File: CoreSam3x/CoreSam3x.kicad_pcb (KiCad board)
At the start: 2 copper layers, 50.8 x 50.8 mm, 65 parts, among them M1 PCB_GREEN_RMC, P1 HDR, P2 HDR, P3 HDR, P4 HDR, P5 HDR, P6 HDR, P8 HDR, Q1 BSS123, U1 ATSAM3X8E, U2 LM1117MP-3.3, U3 USBCONN-HOSTCAPABLE, U4 SP2525A, X1 CRYSTAL_4PIN, X2 32kHz

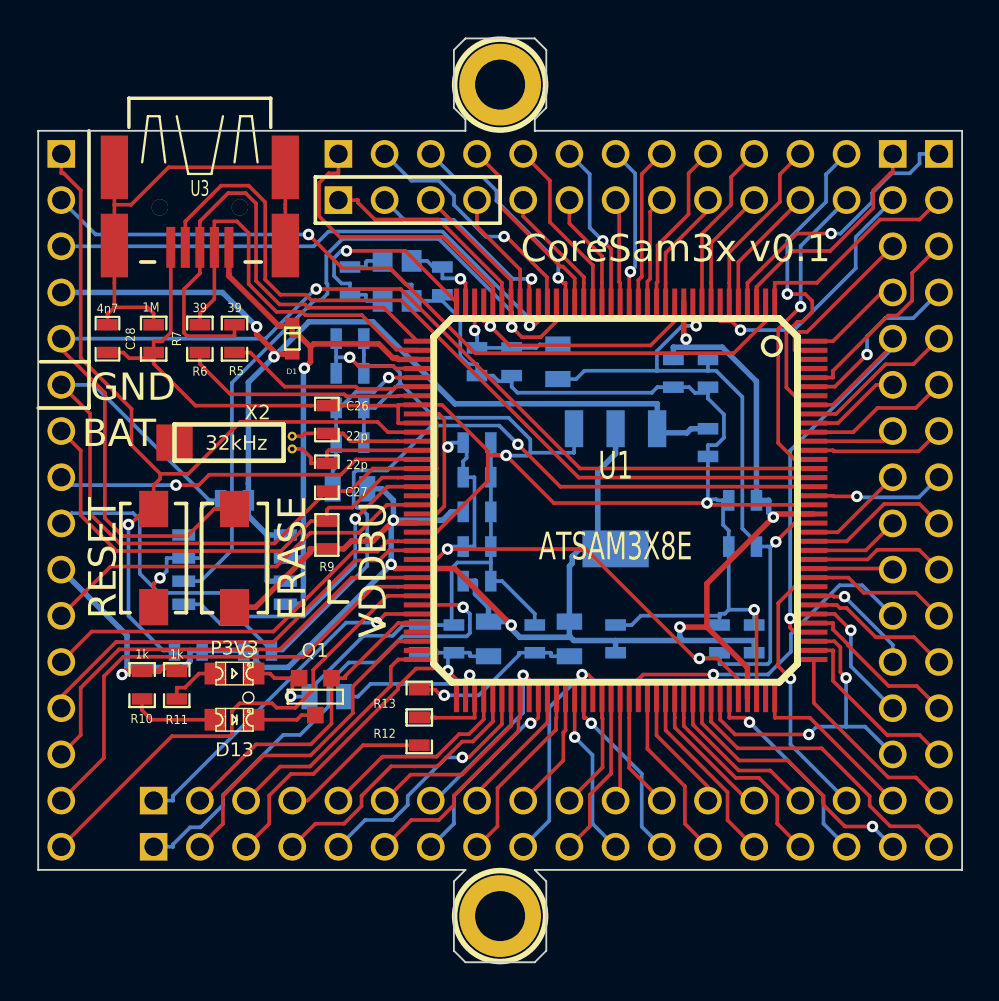
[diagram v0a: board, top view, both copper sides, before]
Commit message: CoreSam3x: improvements to layout, component selection
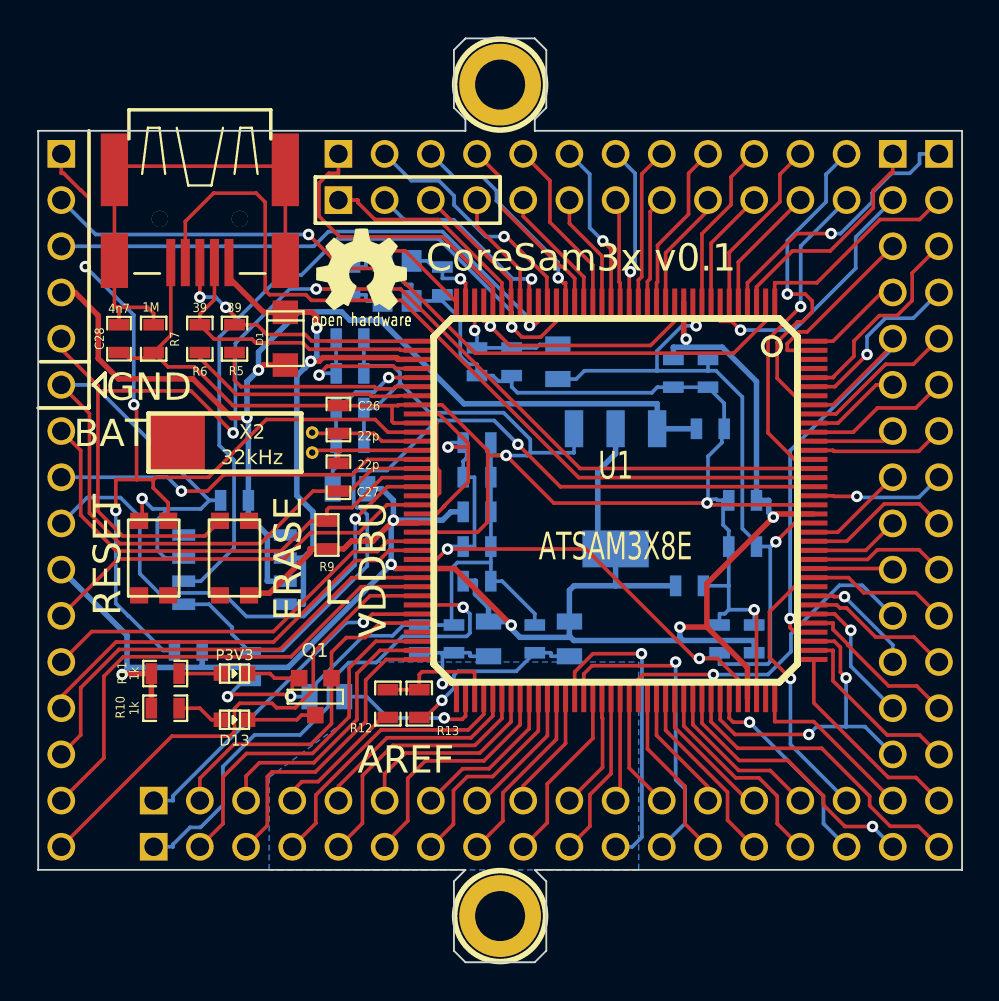
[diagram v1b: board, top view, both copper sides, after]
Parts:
- added M2: LOGO_OSHW, Logo_silk_OSHW_6x6mm, F.Cu at (58.4, 96.5)
- D1: footprint sod523 -> do219ab
- D2: footprint LED-0805_BLUE -> Led_0603
- D3: footprint LED-0805_GREEN -> Led_0603
- R8: value 100k -> 10k
- S1, S2: footprint SW_APEM_ADTSM3 -> SW_C&K_KMR4
- U4: value SP2525A -> SP2525A-1EN
- X2: footprint crystal_tc-26_horiz -> crystal_tc-38_horiz_RMC
- moved C25 5.00 mm to (76.5, 113.9), turned to 0 degrees
- moved R12 2.30 mm to (59.9, 120.4)
- moved R10 1.80 mm to (47.6, 120.7), turned to 0 degrees
- moved R8 0.97 mm to (52.3, 118.4), turned to 90 degrees
- moved R11 0.90 mm to (47.6, 118.7), turned to 0 degrees
- moved C24 0.77 mm to (77.6, 105.3), turned to 0 degrees
- moved U3 0.64 mm to (49.5, 93.3)
- moved C26 0.63 mm to (57.1, 104.8)
- moved C27 0.63 mm to (57.1, 108.0)
- moved C28 0.63 mm to (45.1, 100.3)
- moved D1 0.38 mm to (54.2, 100.3)
- moved X2 0.13 mm to (51.3, 106.0)
- turned R13 to 90 degrees
- turned S1 to 90 degrees
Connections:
- C26 pad 1: N-00000128 -> N-00000126
- P5 pad 3: D43 -> D42
- P5 pad 5: DAC0_CANRX1 -> DAC1
- P6 pad 3: D42 -> D43
- P6 pad 4: DAC1 -> DAC0_CANRX1
- R8 pad 1: UOTGVBOF -> GND
- R8 pad 2: +3.3V -> UOTGVBOF
- U1 pad 48: N-00000128 -> N-00000126
- X2 pad 1: N-00000127 -> N-00000126
- X2 pad 2: N-00000128 -> N-00000127
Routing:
- net DHSDP: track 28.4 -> 15.1 mm, vias 0 -> 2
- net D20_SDA: track 9.08 -> 17.3 mm
- net D21_SCL: track 9.99 -> 17.6 mm
- net N-00000128: track 7.13 -> 0.00 mm
- net N-00000126: track 0.00 -> 5.98 mm
- net DHSDM: track 21.8 -> 16.3 mm
- net DAC0_CANRX1: track 11.0 -> 15.3 mm
- net RESET: track 47.8 -> 51.8 mm, vias 1 -> 3
- net DAC1: track 15.5 -> 11.8 mm
- net D43: track 13.2 -> 16.6 mm
- net ADVREF: track 4.11 -> 7.12 mm
- net ERASE: track 65.6 -> 68.4 mm, vias 1 -> 2
- net A8: track 12.6 -> 9.74 mm, vias 1 -> 0
- net N-0000023: track 4.87 -> 2.26 mm
- net +5V: track 58.1 -> 60.7 mm
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- added copper zone on B.Cu, net VSSA
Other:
- board text added: "AREF"
